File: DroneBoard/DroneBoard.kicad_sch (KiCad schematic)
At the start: 51 parts, among them J1 USB4105-GF-A, J2 Conn_01x02, SW1 1825910-6, SW2 1825910-6, U1 ICM-20608-G, U2 ESP32-S3-WROOM-1-N16, U3 TPS63051RMWR

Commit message: Fixed Schematics
Fixed the flyback diodes
Fixed the LED resistors and extra diodes
Fixed the 0603 sizings
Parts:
- removed D10, D5, D6, D9: 1N4148W, Diode_SMD:D_SOD-123, symbol Diode:1N4148W
- C1, C10, C11, C2, C3, C4, C5, C6, C7, C8, C9, L1: footprint Capacitor_SMD:C_0201_0603Metric_Pad0.64x0.40mm_HandSolder -> Capacitor_SMD:C_0603_1608Metric_Pad1.08x0.95mm_HandSolder
- R1, R2, R3, R4: footprint Resistor_SMD:R_0201_0603Metric -> Resistor_SMD:R_0603_1608Metric_Pad0.98x0.95mm_HandSolder
- R10, R11, R5, R6: value 10k -> 430; footprint Resistor_SMD:R_0201_0603Metric_Pad0.64x0.40mm_HandSolder -> Resistor_SMD:R_0603_1608Metric_Pad0.98x0.95mm_HandSolder
- R12, R7, R8: footprint Resistor_SMD:R_0201_0603Metric_Pad0.64x0.40mm_HandSolder -> Resistor_SMD:R_0603_1608Metric_Pad0.98x0.95mm_HandSolder
- R9: value 5.1 -> 5.1k; footprint Resistor_SMD:R_0201_0603Metric_Pad0.64x0.40mm_HandSolder -> Resistor_SMD:R_0603_1608Metric_Pad0.98x0.95mm_HandSolder
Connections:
- net LED_1: now also LED1.2 (A)
- net LED_2: now also LED2.2 (A)
- net LED_3: now also LED3.2 (A)
- net LED_4: now also LED4.2 (A)
- net VAA: now also D1.1 (K), D2.1 (K), D3.1 (K), D4.1 (K)
- net at Motor4.2 (Pin_2): now also D4.2 (A), MOSFET2.3 (D); no longer D4.1 (K)
- net at Motor3.2 (Pin_2): now also D3.2 (A), MOSFET1.3 (D); no longer D3.1 (K)
- net at D2.2 (A), MOSFET4.3 (D): now also Motor2.2 (Pin_2)
- net at D1.2 (A), MOSFET3.3 (D): now also Motor1.2 (Pin_2)
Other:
- moved on the sheet: D1, D2, D3, D4, Motor3, Motor4

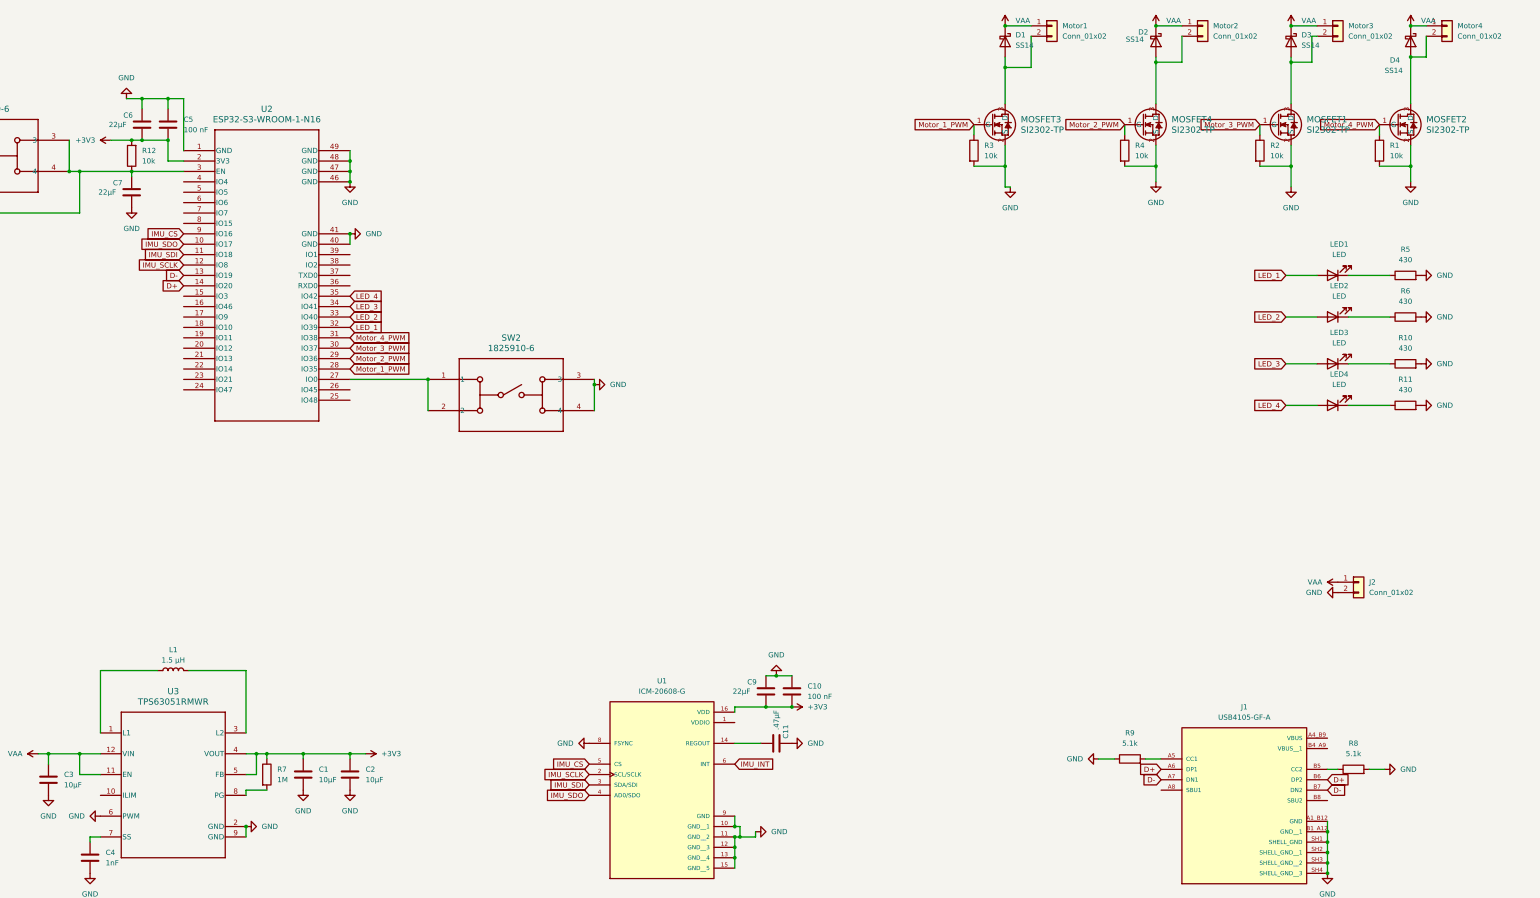
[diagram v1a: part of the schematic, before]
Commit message: Routing and some small schematic updates
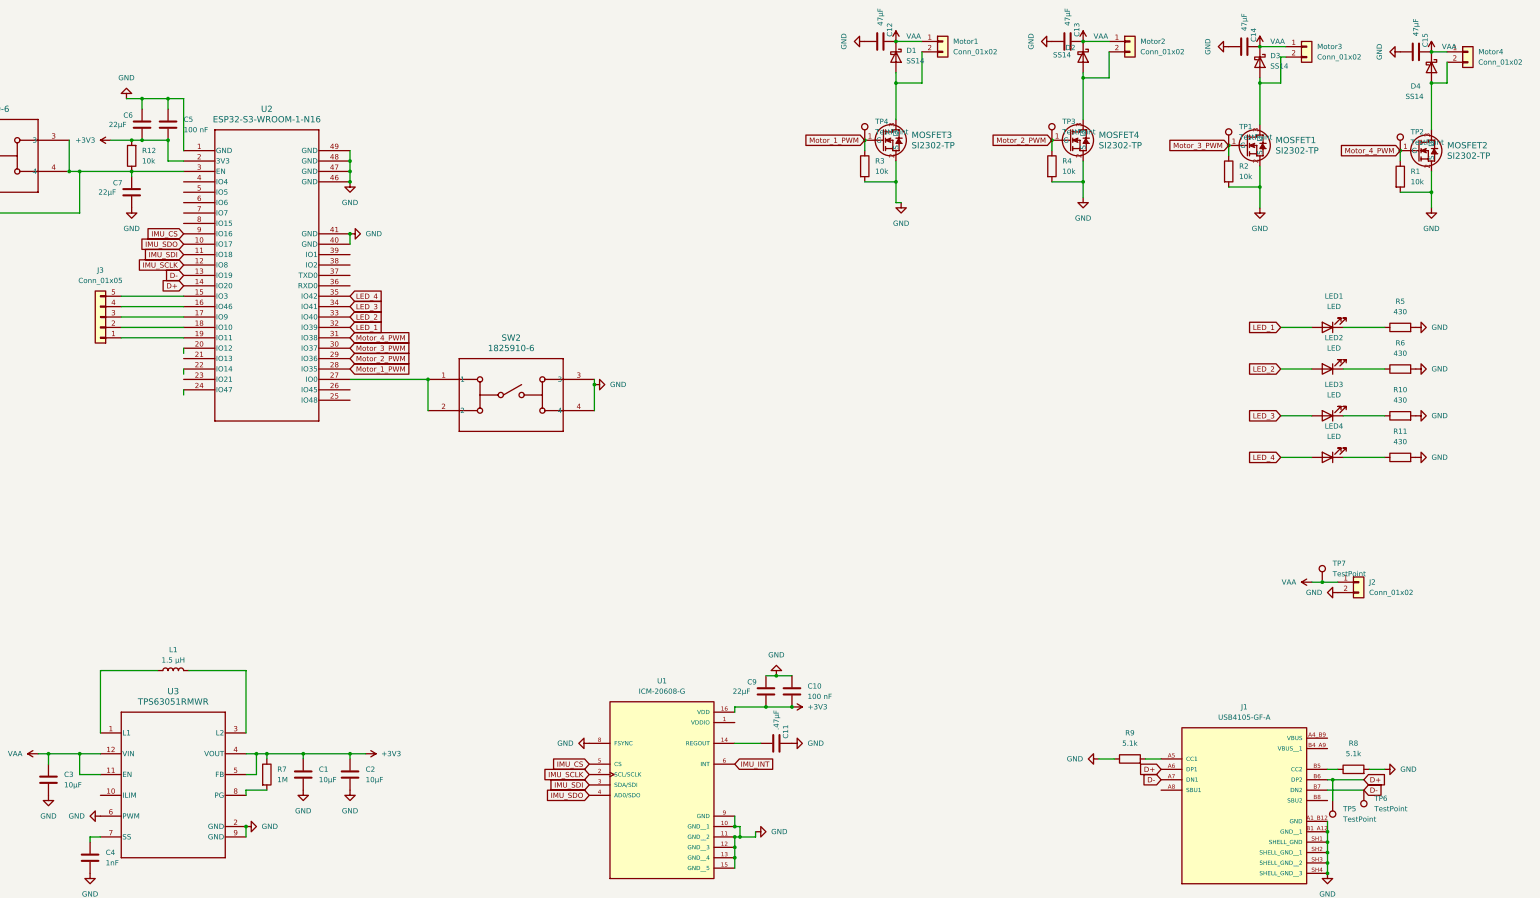
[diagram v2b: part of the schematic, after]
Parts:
- added C12, C13, C14, C15: 47μF, Capacitor_SMD:C_0603_1608Metric_Pad1.08x0.95mm_HandSolder, symbol Device:C
- added J3: Conn_01x05, Connector_PinSocket_2.54mm:PinSocket_1x05_P2.54mm_Vertical, symbol Connector_Generic:Conn_01x05
- added TP1, TP2, TP3, TP4, TP5, TP6, TP7: TestPoint, Connector_Pin:Pin_D1.0mm_L10.0mm, symbol Connector:TestPoint
- LED1, LED2, LED3, LED4: footprint LED_SMD:LED_0201_0603Metric_Pad0.64x0.40mm_HandSolder -> LED_SMD:LED_0603_1608Metric_Pad1.05x0.95mm_HandSolder
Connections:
- net D+: now also TP5.1
- net D-: now also TP6.1
- net GND: now also C12.2, C13.2, C14.2, C15.2
- net Motor_1_PWM: now also TP4.1
- net Motor_2_PWM: now also TP3.1
- net Motor_3_PWM: now also TP1.1
- net Motor_4_PWM: now also TP2.1
- net VAA: now also C12.1, C13.1, C14.1, C15.1, TP7.1
- net at U2.15 (IO3): now also J3.5 (Pin_5)
- net at U2.16 (IO46): now also J3.4 (Pin_4)
- net at U2.17 (IO9): now also J3.3 (Pin_3)
- net at U2.18 (IO10): now also J3.2 (Pin_2)
- net at U2.19 (IO11): now also J3.1 (Pin_1)
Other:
- moved on the sheet: D1, D2, D3, D4, LED1, LED2, LED3, LED4, MOSFET1, MOSFET2, MOSFET3, MOSFET4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

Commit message: Mostly Routing and Power over USBC
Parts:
- added D5: 1N4007, Diode_SMD:D_SMA, symbol Diode:1N4007
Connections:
- net VAA: now also D5.1 (K)
- net at J1.A4_B9 (VBUS): now also J1.B4_A9 (VBUS__1), D5.2 (A)
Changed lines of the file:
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@@
 	)
 	(junction
+		(at 383.54 191.77)
+		(diameter 0)
+		(color 0 0 0 0)
+	)
+	(junction
 		(at 314.96 55.88)
 		(diameter 0)
@@
 	(wire
 		(pts
+			(xy 374.65 194.31) (xy 383.54 194.31)
+		)
+		(stroke
+			(width 0)
+			(type default)
+		)
+	)
+	(wire
+		(pts
 			(xy 374.65 219.71) (xy 374.65 222.25)
 		)
@@
 	(wire
 		(pts
+			(xy 383.54 194.31) (xy 383.54 191.77)
+		)
+		(stroke
+			(width 0)
+			(type default)
+		)
+	)
+	(wire
+		(pts
 			(xy 85.09 35.56) (xy 91.44 35.56)
 		)
@@
 	(wire
 		(pts
+			(xy 374.65 191.77) (xy 383.54 191.77)
+		)
+		(stroke
+			(width 0)
+			(type default)
+		)
+	)
+	(wire
+		(pts
 			(xy 400.05 24.13) (xy 403.86 24.13)
 		)
@@
 	)
 	(symbol
+		(lib_id "Diode:1N4007")
+		(at 387.35 191.77 180)
+		(unit 1)
+		(exclude_from_sim no)
+		(in_bom yes)
+		(on_board yes)
+		(dnp no)
+		(fields_autoplaced yes)
+		(property "Reference" "D5"
+			(at 387.35 185.42 0)
+			(effects
+				(font
+					(size 1.27 1.27)
+				)
+			)
+		)
+		(property "Value" "1N4007"
+			(at 387.35 187.96 0)
+			(effects
+				(font
+					(size 1.27 1.27)
+				)
+			)
+		)
+		(property "Footprint" "Diode_SMD:D_SMA"
+			(at 387.35 187.325 0)
+			(effects
+				(font
+					(size 1.27 1.27)
+				)
+				(hide yes)
+			)
+		)
+		(property "Datasheet" "http://www.vishay.com/docs/88503/1n4001.pdf"
+			(at 387.35 191.77 0)
+			(effects
+				(font
+					(size 1.27 1.27)
+				)
+				(hide yes)
+			)
+		)
+		(property "Description" "1000V 1A General Purpose Rectifier Diode, DO-41"
+			(at 387.35 191.77 0)
+			(effects
+				(font
+					(size 1.27 1.27)
+				)
+				(hide yes)
+			)
+		)
+		(property "Sim.Device" "D"
+			(at 387.35 191.77 0)
+			(effects
+				(font
+					(size 1.27 1.27)
+				)
+				(hide yes)
+			)
+		)
+		(property "Sim.Pins" "1=K 2=A"
+			(at 387.35 191.77 0)
+			(effects
+				(font
+					(size 1.27 1.27)
+				)
+				(hide yes)
+			)
+		)
+		(pin "2"
+		)
+		(pin "1"
+		)
+		(instances
+			(project ""
+				(path "/81ad14fe-aae2-4eb0-86e1-2dd7f9f02de9"
+					(reference "D5")
+					(unit 1)
+				)
+			)
+		)
+	)
+	(symbol
 		(lib_id "power:GND")
 		(at 392.43 24.13 270)
@@
 					(unit 1)
 				)
+			)
+		)
+	)
+	(symbol
+		(lib_id "power:VAA")
+		(at 391.16 191.77 270)
+		(unit 1)
+		(exclude_from_sim no)
+		(in_bom yes)
+		(on_board yes)
+		(dnp no)
+		(fields_autoplaced yes)
+		(property "Reference" "#PWR042"
+			(at 387.35 191.77 0)
+			(effects
+				(font
+					(size 1.27 1.27)
+				)
+				(hide yes)
+			)
+		)
+		(property "Value" "VAA"
+			(at 394.97 191.7699 90)
+			(effects
+				(font
+					(size 1.27 1.27)
+				)
+				(justify left)
+			)
+		)
+		(property "Footprint" ""
+			(at 391.16 191.77 0)
+			(effects
+				(font
+					(size 1.27 1.27)
+				)
+				(hide yes)
+			)
+		)
+		(property "Datasheet" ""
+			(at 391.16 191.77 0)
+			(effects
+				(font
+					(size 1.27 1.27)
+				)
+				(hide yes)
+			)
+		)
+		(property "Description" "Power symbol creates a global label with name \"VAA\""
+			(at 391.16 191.77 0)
+			(effects
+				(font
+					(size 1.27 1.27)
+				)
+				(hide yes)
+			)
+		)
+		(pin "1"
+		)
+		(instances
+			(project "DroneBoard"
+				(path "/81ad14fe-aae2-4eb0-86e1-2dd7f9f02de9"
+					(reference "#PWR042")
+					(unit 1)
+				)
